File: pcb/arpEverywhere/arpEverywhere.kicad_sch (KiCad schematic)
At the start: 56 parts, among them J1 Analog, J2 Digital, J3 DIN-5_180degree, J4 DIN-5_180degree, J5 DIN-5_180degree, J6 DIN-5_180degree, SW1 SW_Rotary_1x12, SW2 SW_Rotary_1x12, SW3 SW_SPDT, SW4 SW_SPDT, SW5 SW_SPDT, SW6 SW_SPDT, U1 6N138, U2 6N138

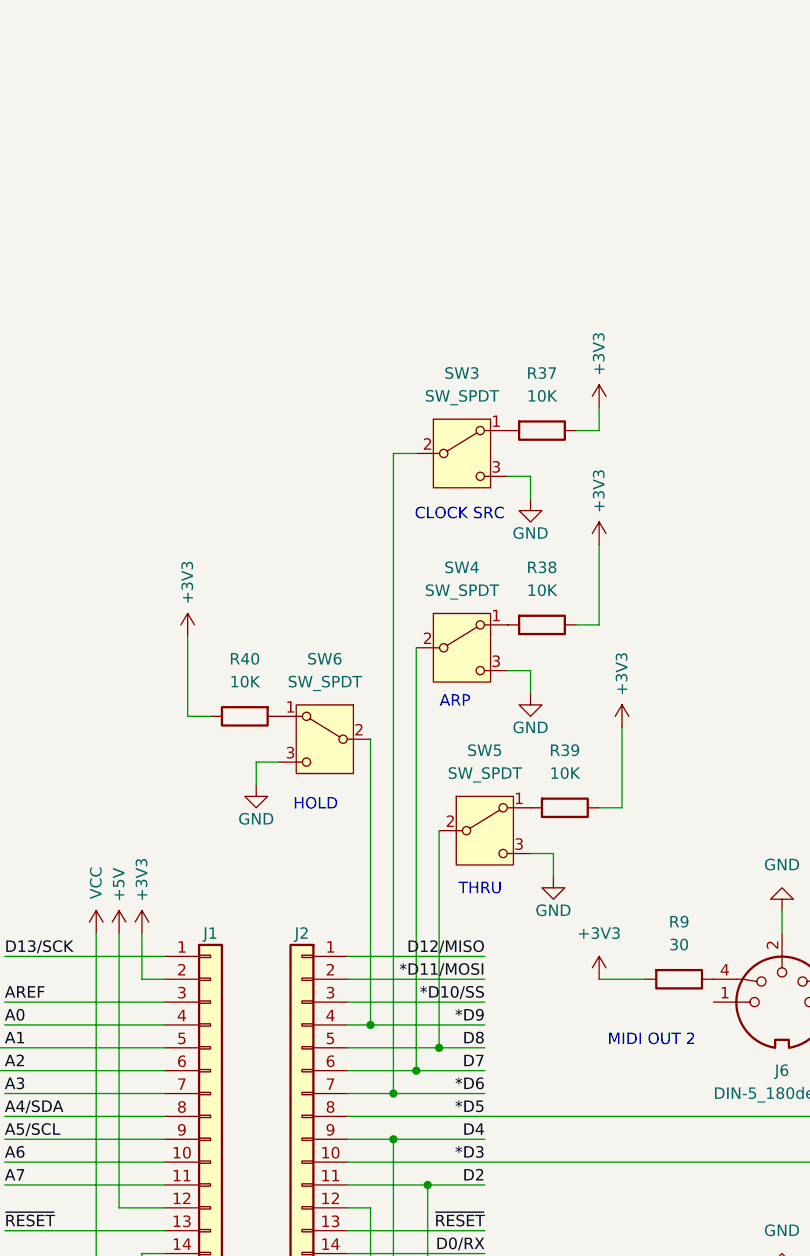
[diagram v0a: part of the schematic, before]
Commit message: fix wrong wiring of input switch circuit
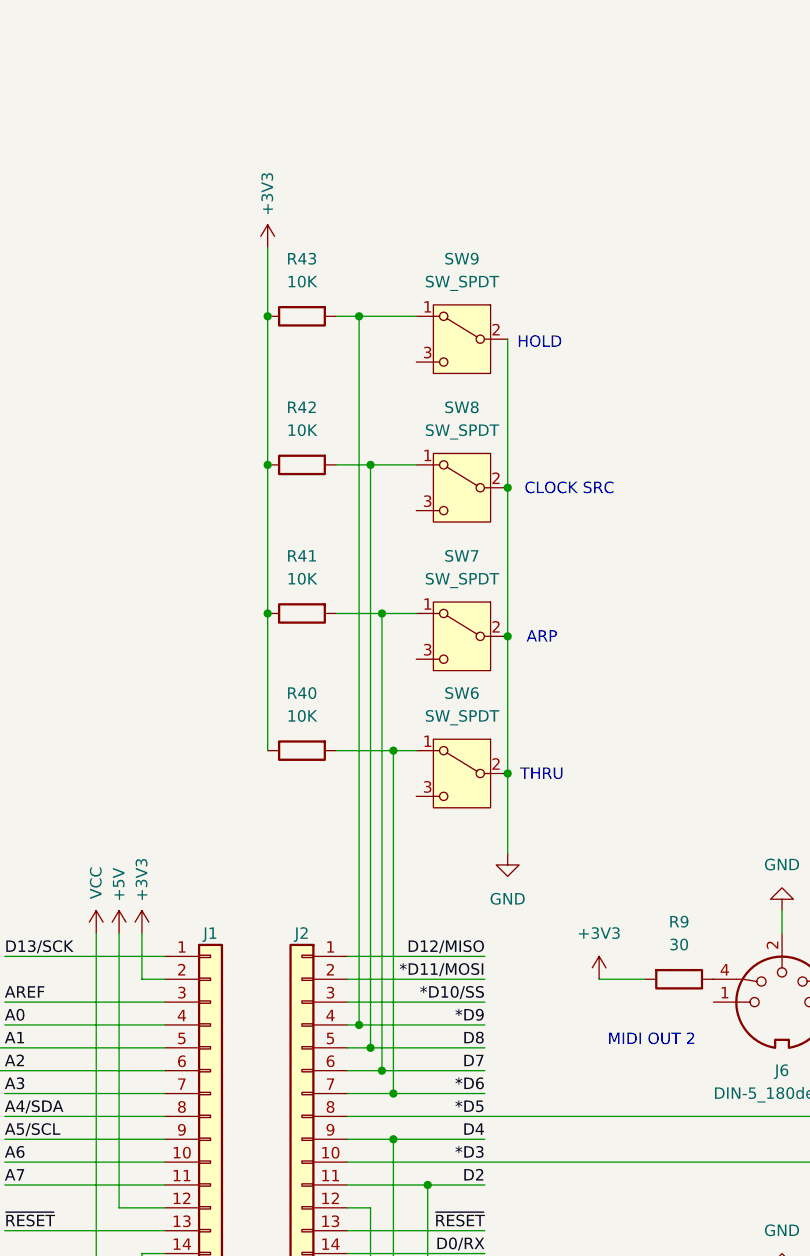
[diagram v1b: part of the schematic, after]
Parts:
- removed R37, R38, R39: 10K, Package_DIP:DIP-8_W7.62mm, symbol Device:R
- removed SW3, SW4, SW5: SW_SPDT, Button_Switch_SMD:Nidec_Copal_CAS-120A, symbol Switch:SW_SPDT
- added R41, R42, R43: 10K, Package_DIP:DIP-8_W7.62mm, symbol Device:R
- added SW7, SW8, SW9: SW_SPDT, Button_Switch_SMD:Nidec_Copal_CAS-120A, symbol Switch:SW_SPDT
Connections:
- net *D6: now also R40.2, SW6.1 (A)
- net *D9: now also R43.2, SW9.1 (A); no longer SW6.2 (B)
- net +3V3: now also R41.1, R42.1, R43.1
- net D7: now also R41.2, SW7.1 (A)
- net D8: now also R42.2, SW8.1 (A)
- net GND: now also SW6.2 (B), SW7.2 (B), SW8.2 (B), SW9.2 (B); no longer SW6.3 (C)
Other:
- moved on the sheet: SW6
